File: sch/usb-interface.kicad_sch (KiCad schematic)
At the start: 8 parts, among them IC1 USB2244I-AEZG-06

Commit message: pågebynt merging av pwr-supply og modem branches
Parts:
- renumbered C21 to C13, C24 to C14, C16 to C15, C23 to C16, C15 to C17, C22 to C18, R17 to R6
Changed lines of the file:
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@@
 	(wire
 		(pts
-			(xy 124.46 97.79) (xy 121.92 97.79)
+			(xy 129.54 97.79) (xy 121.92 97.79)
 		)
 		(stroke
@@
 	(global_label "+3V3_CM5"
 		(shape input)
-		(at 124.46 97.79 0)
+		(at 129.54 97.79 0)
 		(fields_autoplaced yes)
 		(effects
@@
 		)
 		(property "Intersheetrefs" "${INTERSHEET_REFS}"
-			(at 132.5252 97.79 0)
+			(at 137.6052 97.79 0)
 			(effects
 				(font
@@
 		(dnp no)
 		(fields_autoplaced yes)
-		(property "Reference" "C22"
+		(property "Reference" "C18"
 			(at 124.46 99.0662 0)
 			(effects
@@
 			(project "audiograb"
 				(path "/c46c2311-6d4b-411d-b012-c7730eac136d/53f9c81a-1433-4854-9dfc-932cf29aee40"
-					(reference "C22")
+					(reference "C18")
 					(unit 1)
 				)
@@
 		(dnp no)
 		(fields_autoplaced yes)
-		(property "Reference" "C21"
+		(property "Reference" "C13"
 			(at 58.42 99.0662 0)
 			(effects
@@
 			(project "audiograb"
 				(path "/c46c2311-6d4b-411d-b012-c7730eac136d/53f9c81a-1433-4854-9dfc-932cf29aee40"
-					(reference "C21")
+					(reference "C13")
 					(unit 1)
 				)
@@
 		(dnp no)
 		(fields_autoplaced yes)
-		(property "Reference" "#PWR060"
+		(property "Reference" "#PWR040"
 			(at 83.82 160.02 0)
 			(effects
@@
 			(project "audiograb"
 				(path "/c46c2311-6d4b-411d-b012-c7730eac136d/53f9c81a-1433-4854-9dfc-932cf29aee40"
-					(reference "#PWR060")
+					(reference "#PWR040")
 					(unit 1)
 				)
@@
 		(dnp no)
 		(fields_autoplaced yes)
-		(property "Reference" "#PWR032"
+		(property "Reference" "#PWR041"
 			(at 97.79 134.62 0)
 			(effects
@@
 			(project "audiograb"
 				(path "/c46c2311-6d4b-411d-b012-c7730eac136d/53f9c81a-1433-4854-9dfc-932cf29aee40"
-					(reference "#PWR032")
+					(reference "#PWR041")
 					(unit 1)
 				)
@@
 		(dnp no)
 		(fields_autoplaced yes)
-		(property "Reference" "#PWR069"
+		(property "Reference" "#PWR038"
 			(at 73.66 50.8 0)
 			(effects
@@
 			(project "audiograb"
 				(path "/c46c2311-6d4b-411d-b012-c7730eac136d/53f9c81a-1433-4854-9dfc-932cf29aee40"
-					(reference "#PWR069")
+					(reference "#PWR038")
 					(unit 1)
 				)
@@
 		(dnp no)
 		(fields_autoplaced yes)
-		(property "Reference" "C15"
+		(property "Reference" "C17"
 			(at 95.25 46.99 90)
 			(effects
@@
 			(project "audiograb"
 				(path "/c46c2311-6d4b-411d-b012-c7730eac136d/53f9c81a-1433-4854-9dfc-932cf29aee40"
-					(reference "C15")
+					(reference "C17")
 					(unit 1)
 				)
@@
 		(dnp no)
 		(fields_autoplaced yes)
-		(property "Reference" "C24"
+		(property "Reference" "C14"
 			(at 76.2063 36.83 90)
 			(effects
@@
 			(project "audiograb"
 				(path "/c46c2311-6d4b-411d-b012-c7730eac136d/53f9c81a-1433-4854-9dfc-932cf29aee40"
-					(reference "C24")
+					(reference "C14")
 					(unit 1)
 				)
@@
 		(dnp no)
 		(fields_autoplaced yes)
-		(property "Reference" "C23"
+		(property "Reference" "C16"
 			(at 88.9063 128.27 90)
 			(effects
@@
 			(project "audiograb"
 				(path "/c46c2311-6d4b-411d-b012-c7730eac136d/53f9c81a-1433-4854-9dfc-932cf29aee40"
-					(reference "C23")
+					(reference "C16")
 					(unit 1)
 				)
@@
 		(dnp no)
 		(fields_autoplaced yes)
-		(property "Reference" "C16"
+		(property "Reference" "C15"
 			(at 87.63 149.8599 0)
 			(effects
@@
 			(project "audiograb"
 				(path "/c46c2311-6d4b-411d-b012-c7730eac136d/53f9c81a-1433-4854-9dfc-932cf29aee40"
-					(reference "C16")
+					(reference "C15")
 					(unit 1)
 				)
@@
 		(dnp no)
 		(fields_autoplaced yes)
-		(property "Reference" "R17"
+		(property "Reference" "R6"
 			(at 95.25 35.56 90)
 			(effects
@@
 			(project "audiograb"
 				(path "/c46c2311-6d4b-411d-b012-c7730eac136d/53f9c81a-1433-4854-9dfc-932cf29aee40"
-					(reference "R17")
+					(reference "R6")
 					(unit 1)
 				)
@@
 		(dnp no)
 		(fields_autoplaced yes)
-		(property "Reference" "#PWR061"
+		(property "Reference" "#PWR043"
 			(at 99.06 50.8 0)
 			(effects
@@
 			(project "audiograb"
 				(path "/c46c2311-6d4b-411d-b012-c7730eac136d/53f9c81a-1433-4854-9dfc-932cf29aee40"
-					(reference "#PWR061")
+					(reference "#PWR043")
 					(unit 1)
 				)
@@
 		(dnp no)
 		(fields_autoplaced yes)
-		(property "Reference" "#PWR034"
+		(property "Reference" "#PWR044"
 			(at 121.92 109.22 0)
 			(effects
@@
 			(project "audiograb"
 				(path "/c46c2311-6d4b-411d-b012-c7730eac136d/53f9c81a-1433-4854-9dfc-932cf29aee40"
-					(reference "#PWR034")
+					(reference "#PWR044")
 					(unit 1)
 				)
@@
 		(on_board yes)
 		(dnp no)
-		(property "Reference" "#PWR059"
+		(property "Reference" "#PWR039"
 			(at 76.2 50.8 0)
 			(effects
@@
 			(project "audiograb"
 				(path "/c46c2311-6d4b-411d-b012-c7730eac136d/53f9c81a-1433-4854-9dfc-932cf29aee40"
-					(reference "#PWR059")
+					(reference "#PWR039")
 					(unit 1)
 				)
@@
 		(dnp no)
 		(fields_autoplaced yes)
-		(property "Reference" "#PWR058"
+		(property "Reference" "#PWR042"
 			(at 105.41 39.37 0)
 			(effects
@@
 			(project "audiograb"
 				(path "/c46c2311-6d4b-411d-b012-c7730eac136d/53f9c81a-1433-4854-9dfc-932cf29aee40"
-					(reference "#PWR058")
-					(unit 1)
-				)
+					(reference "#PWR042")
+					(unit 1)
+				)

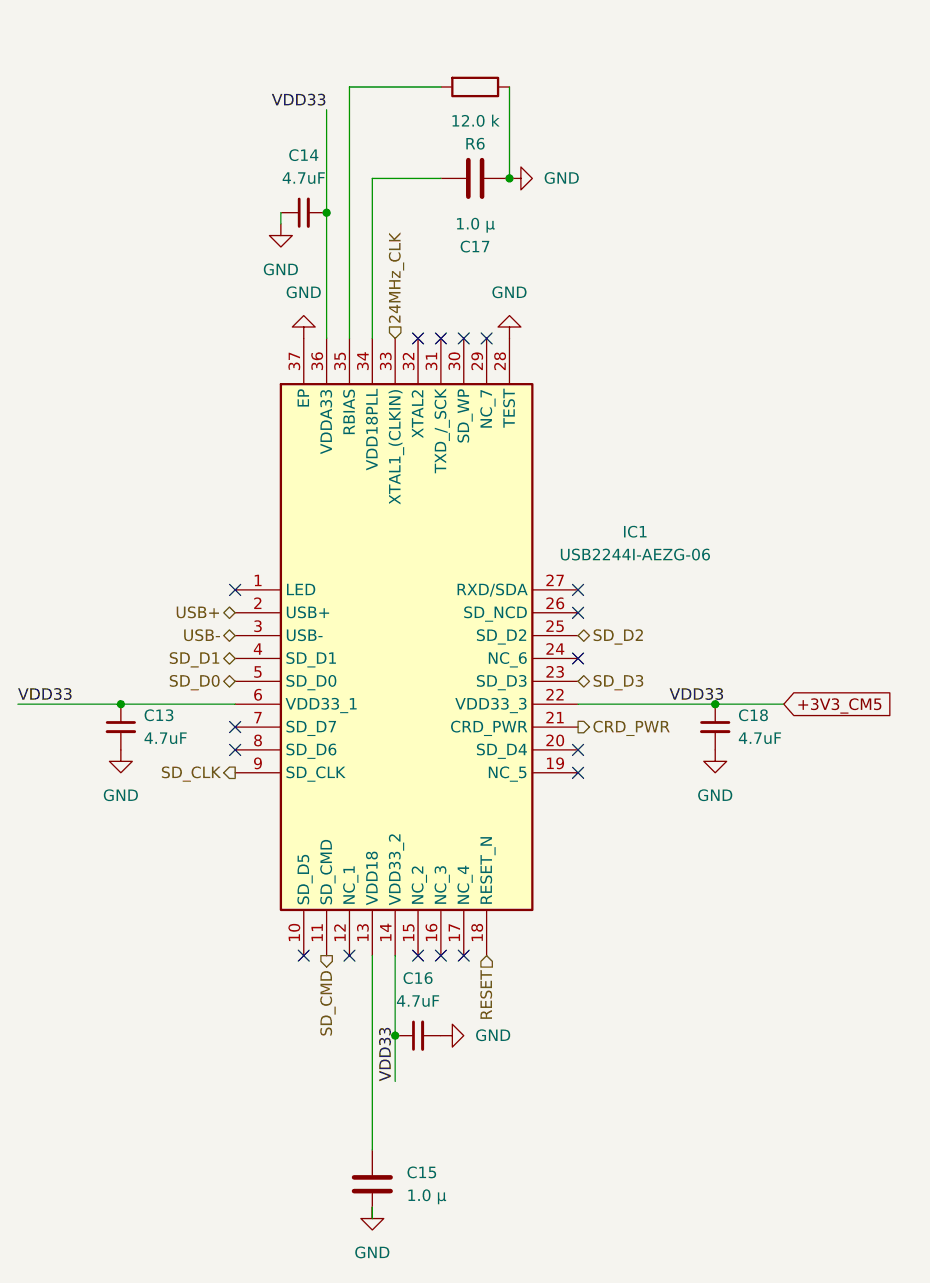
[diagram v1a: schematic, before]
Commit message: lagt inn footprint på alt, obs feil footprint i pwr-supply
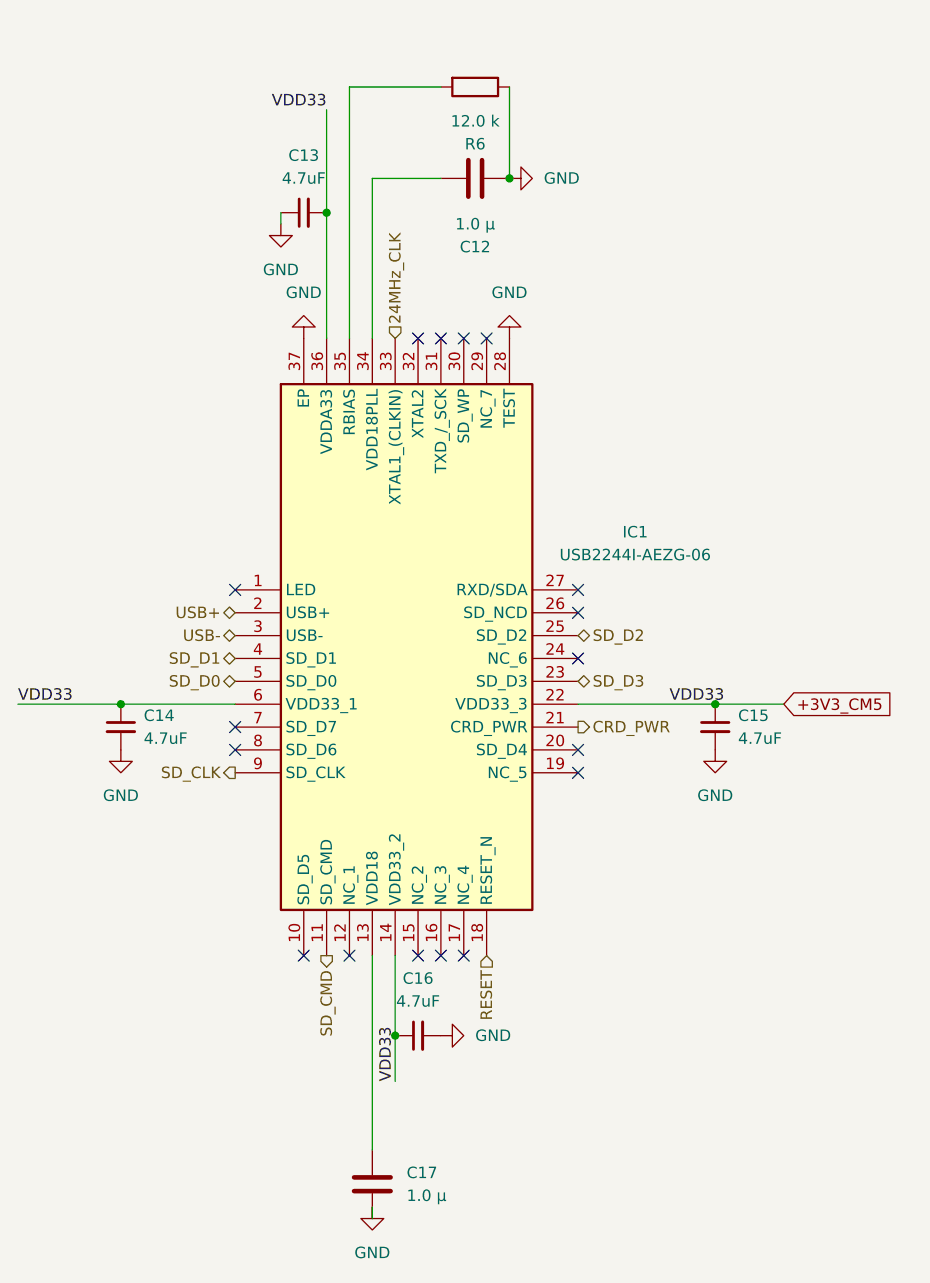
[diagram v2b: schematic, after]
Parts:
- renumbered C17 to C12, C14 to C13, C13 to C14, C18 to C15, C15 to C17
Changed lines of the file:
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@@
 		(dnp no)
 		(fields_autoplaced yes)
-		(property "Reference" "#PWR037"
+		(property "Reference" "#PWR040"
 			(at 55.88 109.22 0)
 			(effects
@@
 			(project "audiograb"
 				(path "/c46c2311-6d4b-411d-b012-c7730eac136d/53f9c81a-1433-4854-9dfc-932cf29aee40"
-					(reference "#PWR037")
+					(reference "#PWR040")
 					(unit 1)
 				)
@@
 		(dnp no)
 		(fields_autoplaced yes)
-		(property "Reference" "C18"
+		(property "Reference" "C15"
 			(at 124.46 99.0662 0)
 			(effects
@@
 			(project "audiograb"
 				(path "/c46c2311-6d4b-411d-b012-c7730eac136d/53f9c81a-1433-4854-9dfc-932cf29aee40"
-					(reference "C18")
+					(reference "C15")
 					(unit 1)
 				)
@@
 		(dnp no)
 		(fields_autoplaced yes)
-		(property "Reference" "C13"
+		(property "Reference" "C14"
 			(at 58.42 99.0662 0)
 			(effects
@@
 			(project "audiograb"
 				(path "/c46c2311-6d4b-411d-b012-c7730eac136d/53f9c81a-1433-4854-9dfc-932cf29aee40"
-					(reference "C13")
+					(reference "C14")
 					(unit 1)
 				)
@@
 		(dnp no)
 		(fields_autoplaced yes)
-		(property "Reference" "#PWR040"
+		(property "Reference" "#PWR043"
 			(at 83.82 160.02 0)
 			(effects
@@
 			(project "audiograb"
 				(path "/c46c2311-6d4b-411d-b012-c7730eac136d/53f9c81a-1433-4854-9dfc-932cf29aee40"
-					(reference "#PWR040")
+					(reference "#PWR043")
 					(unit 1)
 				)
@@
 		(dnp no)
 		(fields_autoplaced yes)
-		(property "Reference" "#PWR041"
+		(property "Reference" "#PWR042"
 			(at 97.79 134.62 0)
 			(effects
@@
 			(project "audiograb"
 				(path "/c46c2311-6d4b-411d-b012-c7730eac136d/53f9c81a-1433-4854-9dfc-932cf29aee40"
-					(reference "#PWR041")
+					(reference "#PWR042")
 					(unit 1)
 				)
@@
 		(dnp no)
 		(fields_autoplaced yes)
-		(property "Reference" "#PWR038"
+		(property "Reference" "#PWR037"
 			(at 73.66 50.8 0)
 			(effects
@@
 			(project "audiograb"
 				(path "/c46c2311-6d4b-411d-b012-c7730eac136d/53f9c81a-1433-4854-9dfc-932cf29aee40"
-					(reference "#PWR038")
+					(reference "#PWR037")
 					(unit 1)
 				)
@@
 		(dnp no)
 		(fields_autoplaced yes)
-		(property "Reference" "C17"
+		(property "Reference" "C12"
 			(at 95.25 46.99 90)
 			(effects
@@
 			(project "audiograb"
 				(path "/c46c2311-6d4b-411d-b012-c7730eac136d/53f9c81a-1433-4854-9dfc-932cf29aee40"
-					(reference "C17")
+					(reference "C12")
 					(unit 1)
 				)
@@
 		(dnp no)
 		(fields_autoplaced yes)
-		(property "Reference" "C14"
+		(property "Reference" "C13"
 			(at 76.2063 36.83 90)
 			(effects
@@
 			(project "audiograb"
 				(path "/c46c2311-6d4b-411d-b012-c7730eac136d/53f9c81a-1433-4854-9dfc-932cf29aee40"
-					(reference "C14")
+					(reference "C13")
 					(unit 1)
 				)
@@
 		(dnp no)
 		(fields_autoplaced yes)
-		(property "Reference" "C15"
+		(property "Reference" "C17"
 			(at 87.63 149.8599 0)
 			(effects
@@
 			(project "audiograb"
 				(path "/c46c2311-6d4b-411d-b012-c7730eac136d/53f9c81a-1433-4854-9dfc-932cf29aee40"
-					(reference "C15")
+					(reference "C17")
 					(unit 1)
 				)
@@
 		(dnp no)
 		(fields_autoplaced yes)
-		(property "Reference" "#PWR043"
+		(property "Reference" "#PWR039"
 			(at 99.06 50.8 0)
 			(effects
@@
 			(project "audiograb"
 				(path "/c46c2311-6d4b-411d-b012-c7730eac136d/53f9c81a-1433-4854-9dfc-932cf29aee40"
-					(reference "#PWR043")
+					(reference "#PWR039")
 					(unit 1)
 				)
@@
 		(dnp no)
 		(fields_autoplaced yes)
-		(property "Reference" "#PWR044"
+		(property "Reference" "#PWR041"
 			(at 121.92 109.22 0)
 			(effects
@@
 			(project "audiograb"
 				(path "/c46c2311-6d4b-411d-b012-c7730eac136d/53f9c81a-1433-4854-9dfc-932cf29aee40"
-					(reference "#PWR044")
+					(reference "#PWR041")
 					(unit 1)
 				)
@@
 		(on_board yes)
 		(dnp no)
-		(property "Reference" "#PWR039"
+		(property "Reference" "#PWR038"
 			(at 76.2 50.8 0)
 			(effects
@@
 			(project "audiograb"
 				(path "/c46c2311-6d4b-411d-b012-c7730eac136d/53f9c81a-1433-4854-9dfc-932cf29aee40"
-					(reference "#PWR039")
+					(reference "#PWR038")
 					(unit 1)
 				)
@@
 		(dnp no)
 		(fields_autoplaced yes)
-		(property "Reference" "#PWR042"
+		(property "Reference" "#PWR036"
 			(at 105.41 39.37 0)
 			(effects
@@
 			(project "audiograb"
 				(path "/c46c2311-6d4b-411d-b012-c7730eac136d/53f9c81a-1433-4854-9dfc-932cf29aee40"
-					(reference "#PWR042")
-					(unit 1)
-				)
+					(reference "#PWR036")
+					(unit 1)
+				)

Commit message: Ferdig pcb-layout modem og simkort, ikke kobla til CM enda
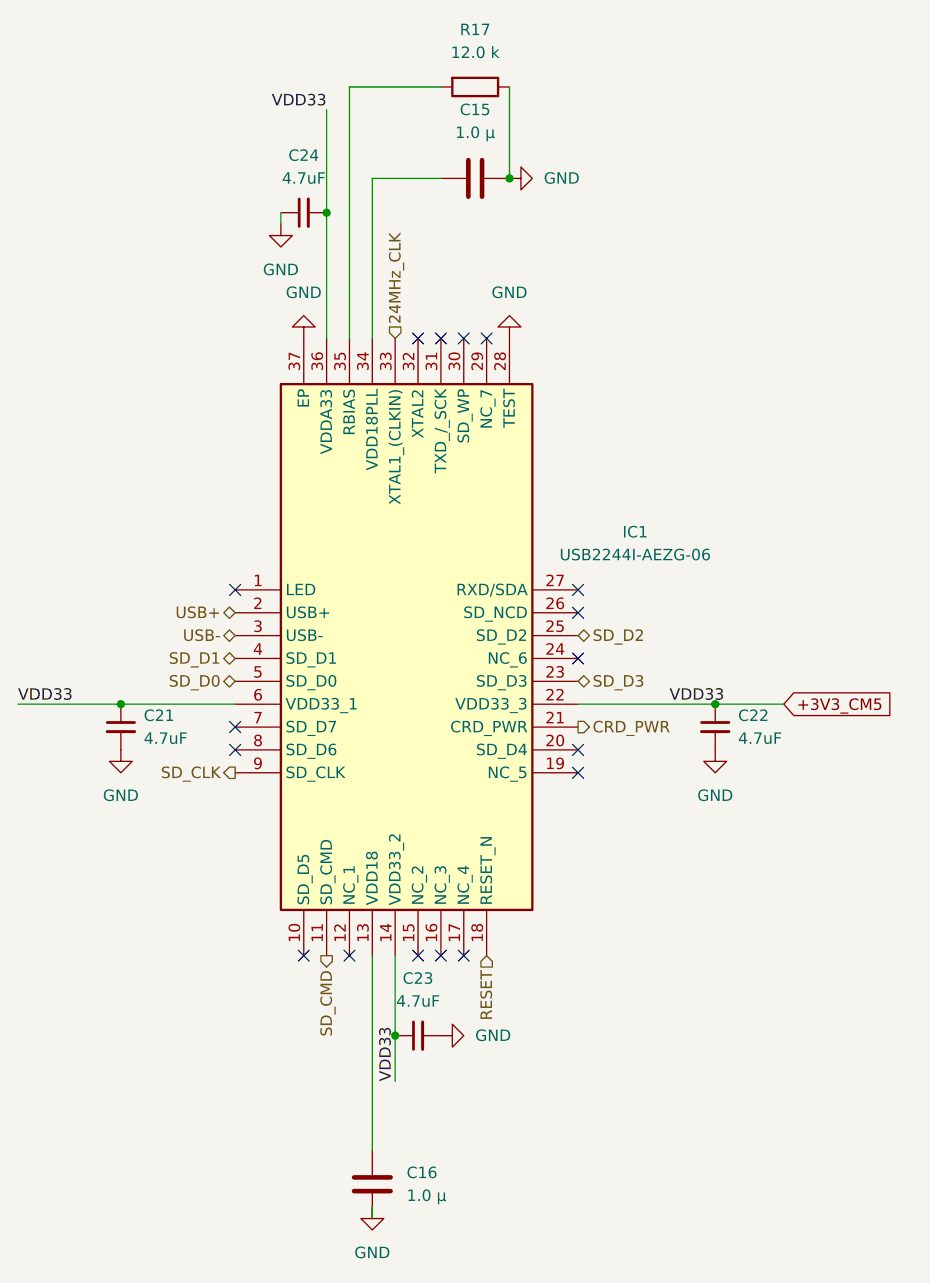
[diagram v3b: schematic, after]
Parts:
- renumbered C12 to C15, C17 to C16, C14 to C21, C15 to C22, C16 to C23, C13 to C24, R6 to R17
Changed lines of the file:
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@@
 		(dnp no)
 		(fields_autoplaced yes)
-		(property "Reference" "C15"
+		(property "Reference" "C22"
 			(at 124.46 99.0662 0)
 			(effects
@@
 			(project "audiograb"
 				(path "/c46c2311-6d4b-411d-b012-c7730eac136d/53f9c81a-1433-4854-9dfc-932cf29aee40"
-					(reference "C15")
+					(reference "C22")
 					(unit 1)
 				)
@@
 		(dnp no)
 		(fields_autoplaced yes)
-		(property "Reference" "C14"
+		(property "Reference" "C21"
 			(at 58.42 99.0662 0)
 			(effects
@@
 			(project "audiograb"
 				(path "/c46c2311-6d4b-411d-b012-c7730eac136d/53f9c81a-1433-4854-9dfc-932cf29aee40"
-					(reference "C14")
+					(reference "C21")
 					(unit 1)
 				)
@@
 		(dnp no)
 		(fields_autoplaced yes)
-		(property "Reference" "C12"
-			(at 95.25 46.99 90)
+		(property "Reference" "C15"
+			(at 95.25 31.75 90)
 			(effects
 				(font
@@
 		)
 		(property "Value" "1.0 µ"
-			(at 95.25 44.45 90)
+			(at 95.25 34.29 90)
 			(effects
 				(font
@@
 			(project "audiograb"
 				(path "/c46c2311-6d4b-411d-b012-c7730eac136d/53f9c81a-1433-4854-9dfc-932cf29aee40"
-					(reference "C12")
+					(reference "C15")
 					(unit 1)
 				)
@@
 		(dnp no)
 		(fields_autoplaced yes)
-		(property "Reference" "C13"
+		(property "Reference" "C24"
 			(at 76.2063 36.83 90)
 			(effects
@@
 			(project "audiograb"
 				(path "/c46c2311-6d4b-411d-b012-c7730eac136d/53f9c81a-1433-4854-9dfc-932cf29aee40"
-					(reference "C13")
+					(reference "C24")
 					(unit 1)
 				)
@@
 		(dnp no)
 		(fields_autoplaced yes)
-		(property "Reference" "C16"
+		(property "Reference" "C23"
 			(at 88.9063 128.27 90)
 			(effects
@@
 			(project "audiograb"
 				(path "/c46c2311-6d4b-411d-b012-c7730eac136d/53f9c81a-1433-4854-9dfc-932cf29aee40"
-					(reference "C16")
+					(reference "C23")
 					(unit 1)
 				)
@@
 		(dnp no)
 		(fields_autoplaced yes)
-		(property "Reference" "C17"
+		(property "Reference" "C16"
 			(at 87.63 149.8599 0)
 			(effects
@@
 			(project "audiograb"
 				(path "/c46c2311-6d4b-411d-b012-c7730eac136d/53f9c81a-1433-4854-9dfc-932cf29aee40"
-					(reference "C17")
+					(reference "C16")
 					(unit 1)
 				)
@@
 		(dnp no)
 		(fields_autoplaced yes)
-		(property "Reference" "R6"
-			(at 95.25 35.56 90)
+		(property "Reference" "R17"
+			(at 95.25 22.86 90)
 			(effects
 				(font
@@
 		)
 		(property "Value" "12.0 k"
-			(at 95.25 33.02 90)
+			(at 95.25 25.4 90)
 			(effects
 				(font
@@
 			(project "audiograb"
 				(path "/c46c2311-6d4b-411d-b012-c7730eac136d/53f9c81a-1433-4854-9dfc-932cf29aee40"
-					(reference "R6")
-					(unit 1)
-				)
+					(reference "R17")
+					(unit 1)
+				)

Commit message: partnumber, manufaturerer and description cleanup completed
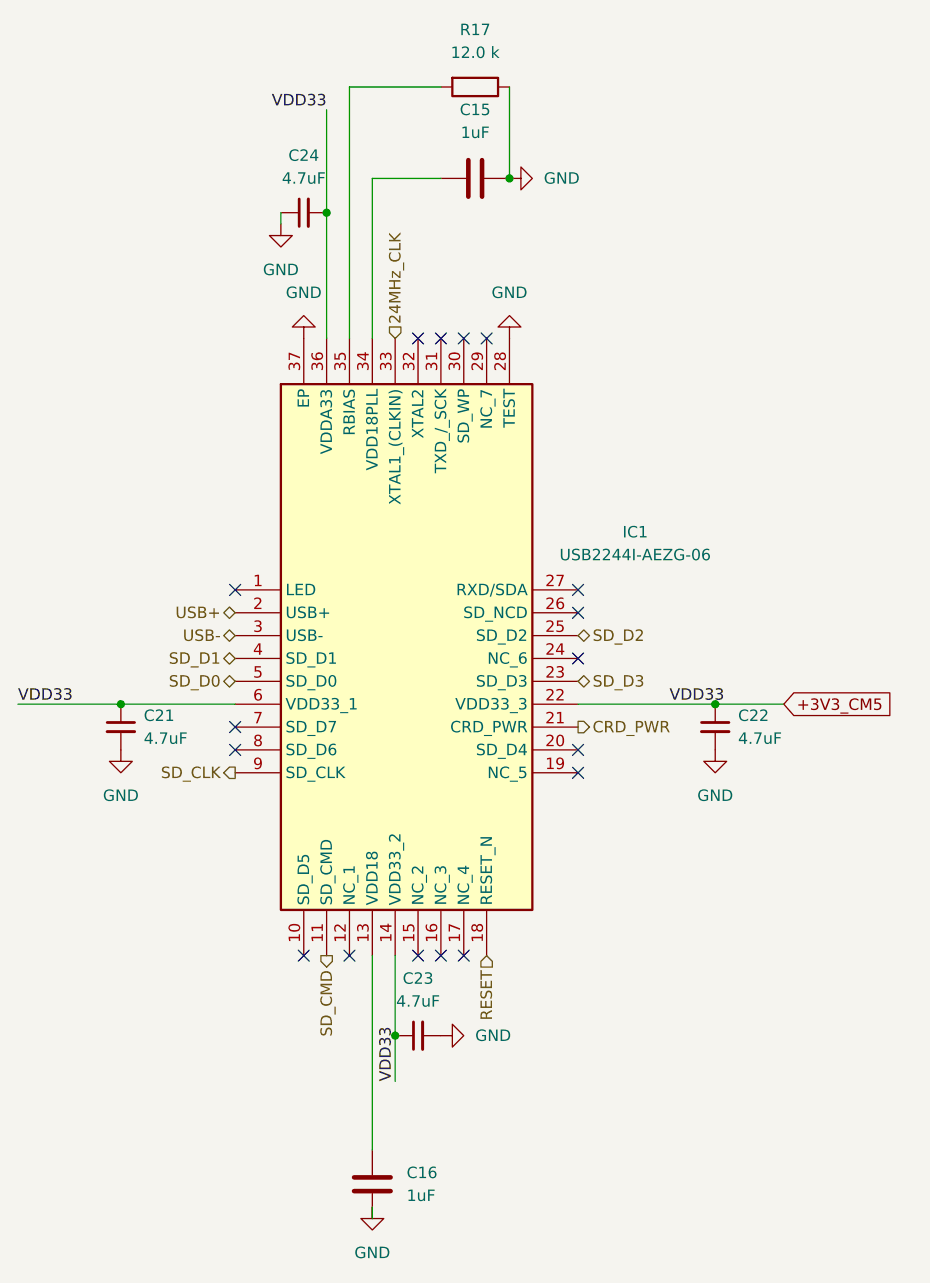
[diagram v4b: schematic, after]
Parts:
- C15, C16: value 1.0 µ -> 1uF
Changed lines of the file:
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@@
 			)
 		)
-		(property "Value" "1.0 µ"
+		(property "Value" "1uF"
 			(at 95.25 34.29 90)
 			(effects
@@
 			)
 		)
-		(property "Value" "1.0 µ"
+		(property "Value" "1uF"
 			(at 87.63 152.3999 0)
 			(effects
